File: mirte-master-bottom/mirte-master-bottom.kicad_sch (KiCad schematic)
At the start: 9 parts, among them J13 oled_conn, Q1 DMG2305UX

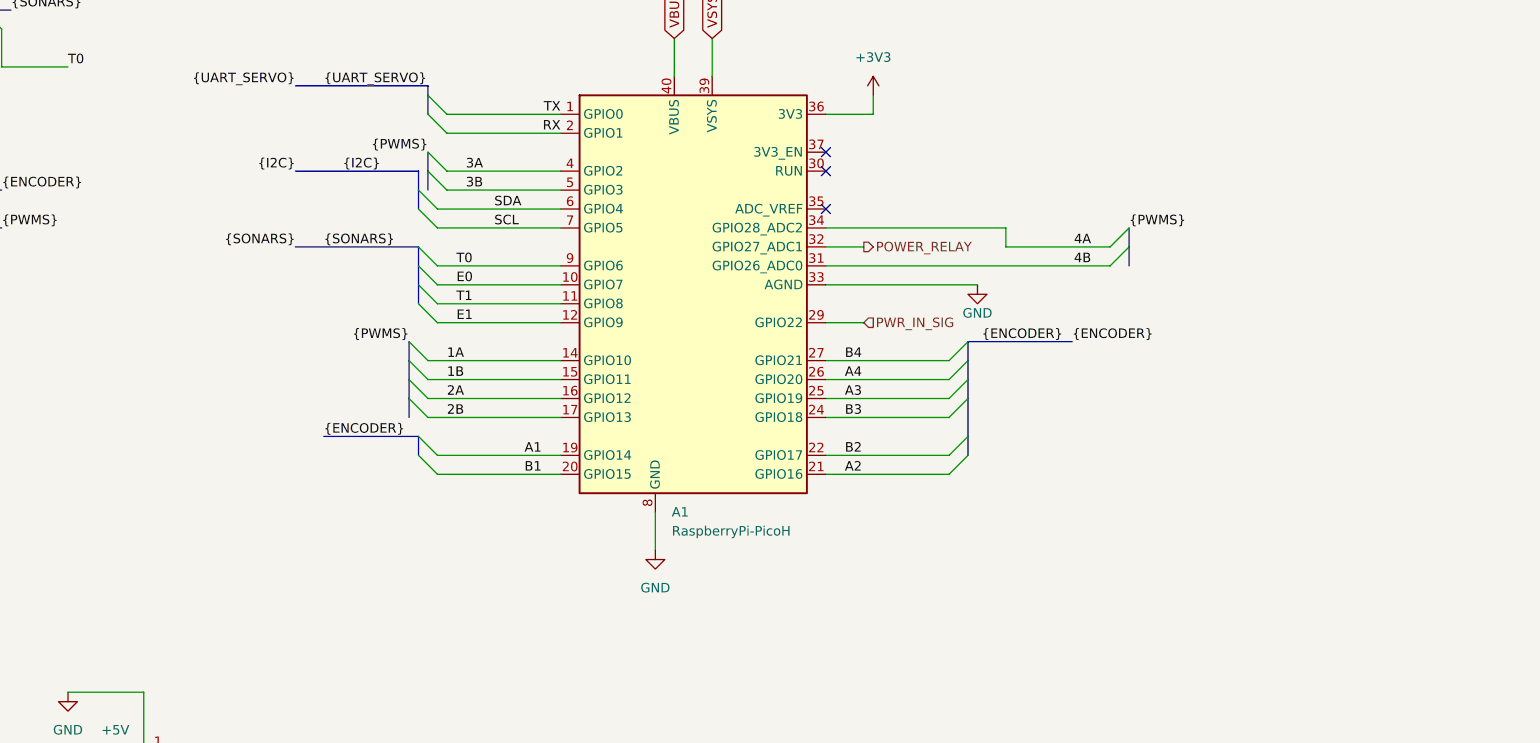
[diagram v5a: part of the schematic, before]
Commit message: ordered pcb main v3
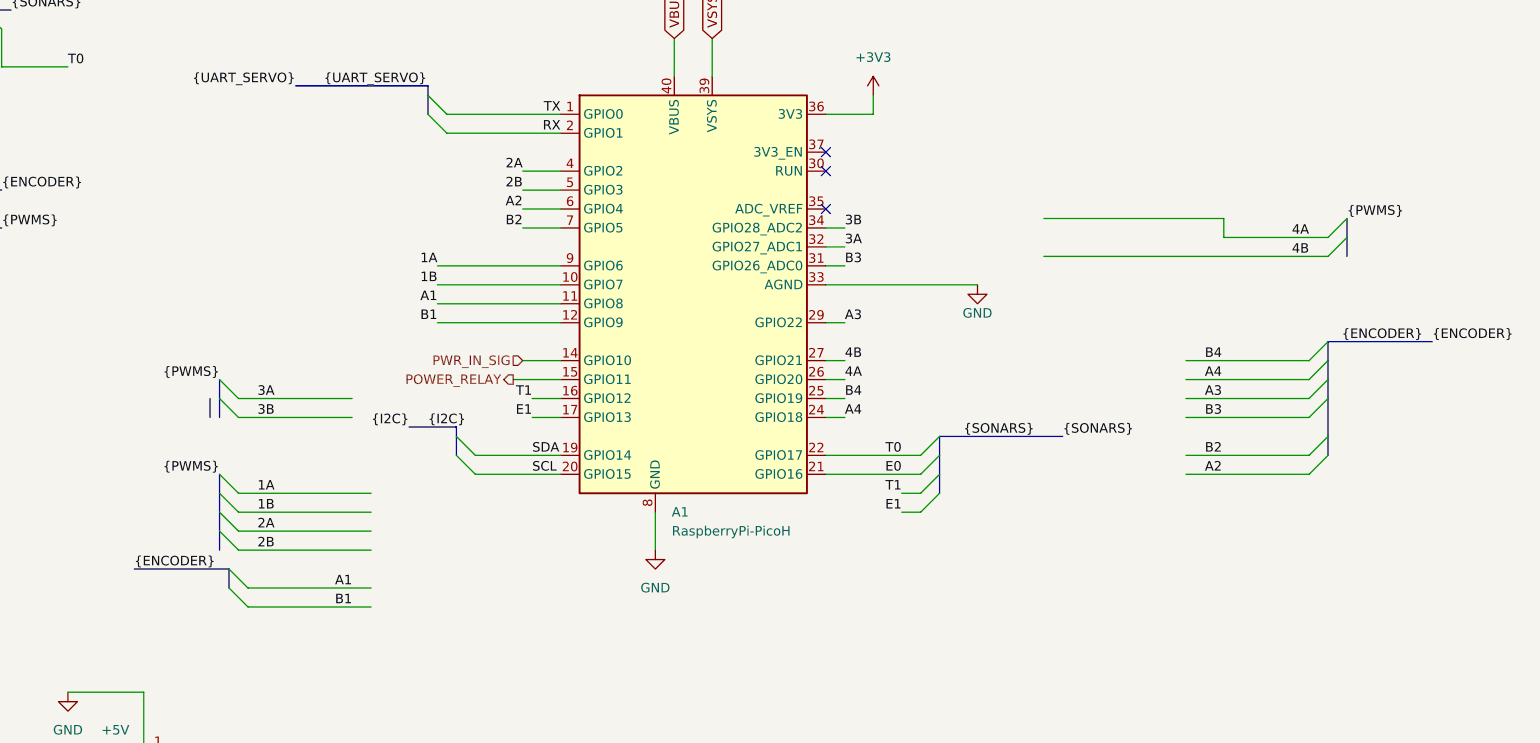
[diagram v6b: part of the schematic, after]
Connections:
- net 1A: now also A1.9 (GPIO6); no longer A1.14 (GPIO10)
- net 1B: now also A1.10 (GPIO7); no longer A1.15 (GPIO11)
- net 2A: now also A1.4 (GPIO2); no longer A1.16 (GPIO12)
- net 2B: now also A1.5 (GPIO3); no longer A1.17 (GPIO13)
- net 3A: now also A1.32 (GPIO27_ADC1); no longer A1.4 (GPIO2)
- net 3B: now also A1.34 (GPIO28_ADC2); no longer A1.5 (GPIO3)
- net 4A: now also A1.26 (GPIO20); no longer A1.34 (GPIO28_ADC2)
- net 4B: now also A1.27 (GPIO21); no longer A1.31 (GPIO26_ADC0)
- net A1: now also A1.11 (GPIO8); no longer A1.19 (GPIO14)
- net A2: now also A1.6 (GPIO4); no longer A1.21 (GPIO16)
- net A3: now also A1.29 (GPIO22); no longer A1.25 (GPIO19)
- net A4: now also A1.24 (GPIO18); no longer A1.26 (GPIO20)
- net B1: now also A1.12 (GPIO9); no longer A1.20 (GPIO15)
- net B2: now also A1.7 (GPIO5); no longer A1.22 (GPIO17)
- net B3: now also A1.31 (GPIO26_ADC0); no longer A1.24 (GPIO18)
- net B4: now also A1.25 (GPIO19); no longer A1.27 (GPIO21)
- net E0: now also A1.21 (GPIO16); no longer A1.10 (GPIO7)
- net E1: now also A1.17 (GPIO13); no longer A1.12 (GPIO9)
- net POWER_RELAY: now also A1.15 (GPIO11); no longer A1.32 (GPIO27_ADC1)
- net PWR_IN_SIG: now also A1.14 (GPIO10); no longer A1.29 (GPIO22)
- net SCL: now also A1.20 (GPIO15); no longer A1.7 (GPIO5)
- net SDA: now also A1.19 (GPIO14); no longer A1.6 (GPIO4)
- net T0: now also A1.22 (GPIO17); no longer A1.9 (GPIO6)
- net T1: now also A1.16 (GPIO12); no longer A1.11 (GPIO8)

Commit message: first reorder pico
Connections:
- net 1A: no longer A1.9 (GPIO6)
- net 1B: no longer A1.10 (GPIO7)
- net 2A: no longer A1.4 (GPIO2)
- net 2B: no longer A1.5 (GPIO3)
- net 3A: no longer A1.32 (GPIO27_ADC1)
- net 3B: no longer A1.34 (GPIO28_ADC2)
- net 4A: now also A1.5 (GPIO3); no longer A1.26 (GPIO20)
- net 4B: now also A1.4 (GPIO2); no longer A1.27 (GPIO21)
- net A1: no longer A1.11 (GPIO8)
- net A2: no longer A1.6 (GPIO4)
- net A3: no longer A1.29 (GPIO22)
- net A4: now also A1.7 (GPIO5); no longer A1.24 (GPIO18)
- net B1: no longer A1.12 (GPIO9)
- net B2: no longer A1.7 (GPIO5)
- net B3: no longer A1.31 (GPIO26_ADC0)
- net B4: now also A1.6 (GPIO4); no longer A1.25 (GPIO19)
- net E0: no longer A1.21 (GPIO16)
- net E1: no longer A1.17 (GPIO13)
- net POWER_RELAY: no longer A1.15 (GPIO11)
- net PWR_IN_SIG: no longer A1.14 (GPIO10)
- net T0: no longer A1.22 (GPIO17)
- net T1: no longer A1.16 (GPIO12)

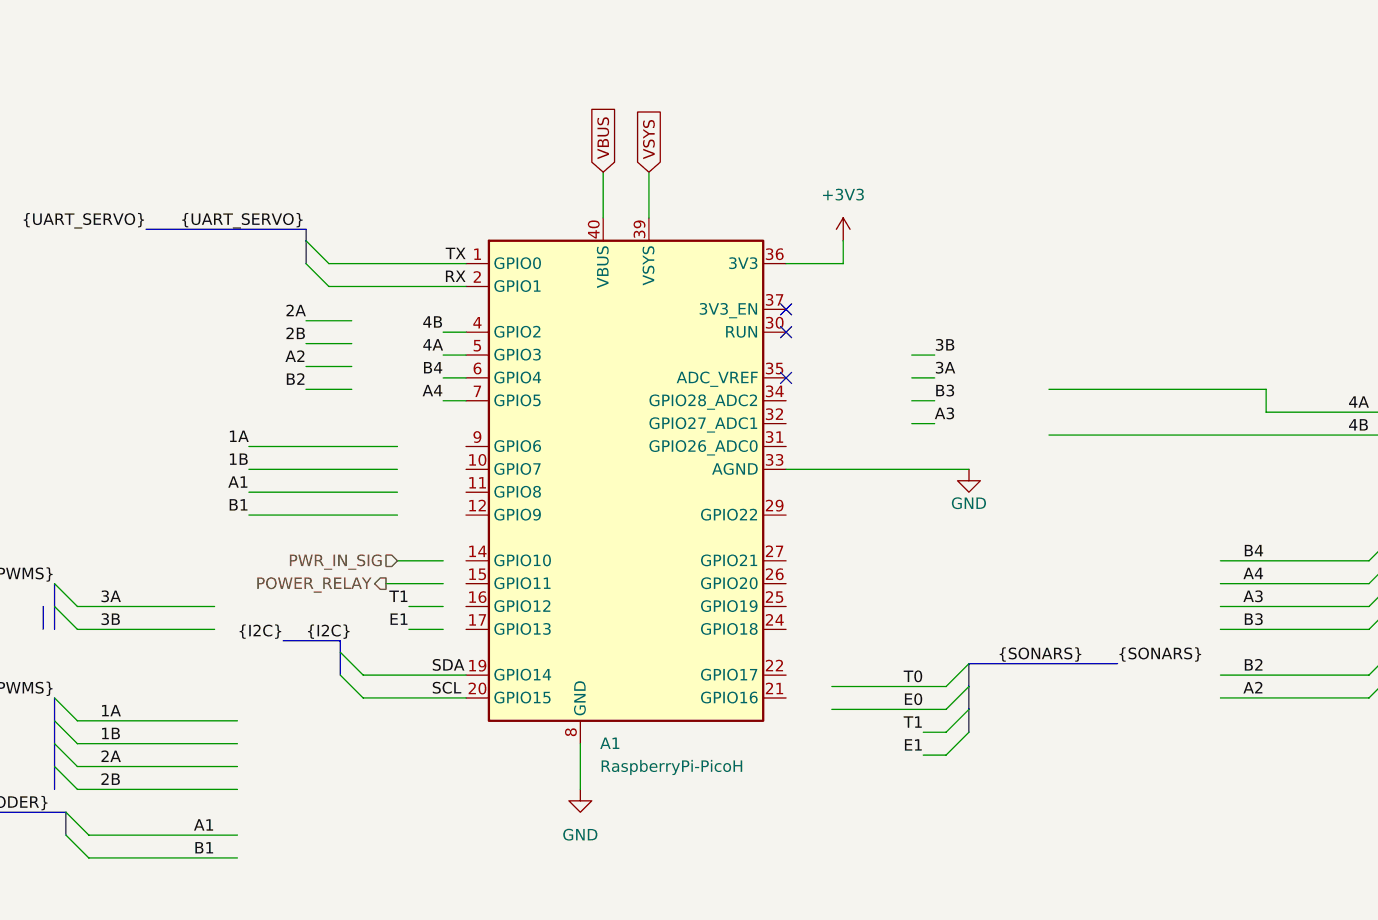
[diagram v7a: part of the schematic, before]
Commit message: pico reorder done, todo reorder 2 for i2c at bottom
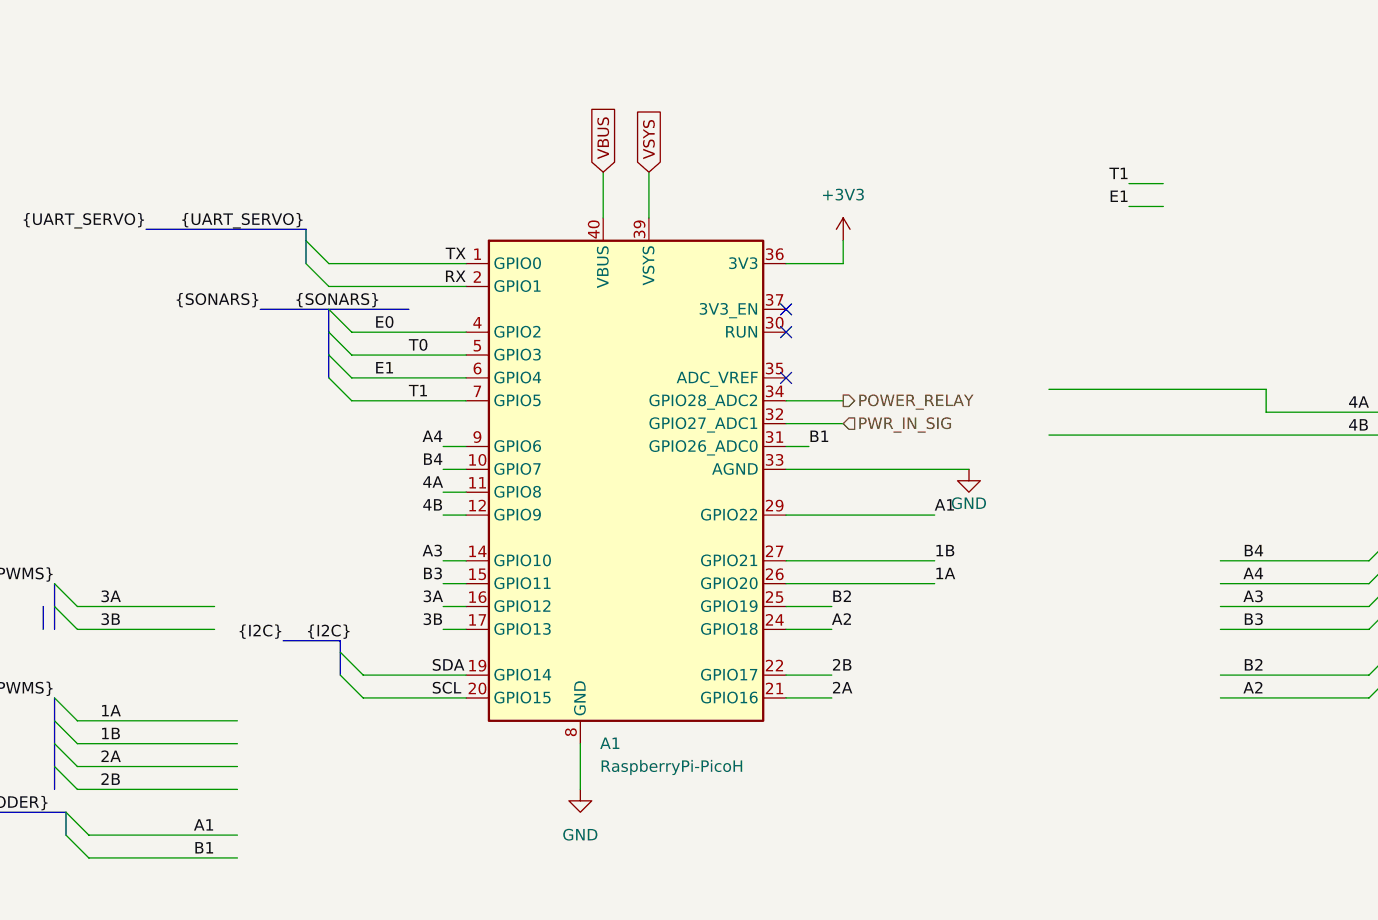
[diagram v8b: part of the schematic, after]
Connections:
- net 1A: now also A1.26 (GPIO20)
- net 1B: now also A1.27 (GPIO21)
- net 2A: now also A1.21 (GPIO16)
- net 2B: now also A1.22 (GPIO17)
- net 3A: now also A1.16 (GPIO12)
- net 3B: now also A1.17 (GPIO13)
- net 4A: now also A1.11 (GPIO8); no longer A1.5 (GPIO3)
- net 4B: now also A1.12 (GPIO9); no longer A1.4 (GPIO2)
- net A1: now also A1.29 (GPIO22)
- net A2: now also A1.24 (GPIO18)
- net A3: now also A1.14 (GPIO10)
- net A4: now also A1.9 (GPIO6); no longer A1.7 (GPIO5)
- net B1: now also A1.31 (GPIO26_ADC0)
- net B2: now also A1.25 (GPIO19)
- net B3: now also A1.15 (GPIO11)
- net B4: now also A1.10 (GPIO7); no longer A1.6 (GPIO4)
- net E0: now also A1.4 (GPIO2)
- net E1: now also A1.6 (GPIO4)
- net POWER_RELAY: now also A1.34 (GPIO28_ADC2)
- net PWR_IN_SIG: now also A1.32 (GPIO27_ADC1)
- net T0: now also A1.5 (GPIO3)
- net T1: now also A1.7 (GPIO5)
